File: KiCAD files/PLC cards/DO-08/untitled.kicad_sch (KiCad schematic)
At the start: 50 parts

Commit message: pcbs
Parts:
- gave numbers to parts that had none: 50

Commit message: pcbs
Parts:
- RN2, RN3: value 220 -> (none)
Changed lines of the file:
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@@
   (symbol (lib_id "Device:R_Network04") (at 200.66 24.638 0) (unit 1)
     (in_bom yes) (on_board yes) (fields_autoplaced)
-    (property "Reference" "RN3" (id 0) (at 205.232 23.6219 0)
+    (property "Reference" "RN3" (id 0) (at 205.74 23.6219 0)
       (effects (font (size 1.27 1.27)) (justify left))
     )
-    (property "Value" "220" (id 1) (at 205.232 26.1619 0)
+    (property "Value" "" (id 1) (at 205.74 26.1619 0)
       (effects (font (size 1.27 1.27)) (justify left))
     )
@@
   (symbol (lib_id "Device:R_Network04") (at 67.31 68.326 0) (unit 1)
     (in_bom yes) (on_board yes) (fields_autoplaced)
-    (property "Reference" "RN2" (id 0) (at 71.882 67.3099 0)
+    (property "Reference" "RN2" (id 0) (at 72.39 67.3099 0)
       (effects (font (size 1.27 1.27)) (justify left))
     )
-    (property "Value" "220" (id 1) (at 71.882 69.8499 0)
+    (property "Value" "" (id 1) (at 72.39 69.8499 0)
       (effects (font (size 1.27 1.27)) (justify left))
     )

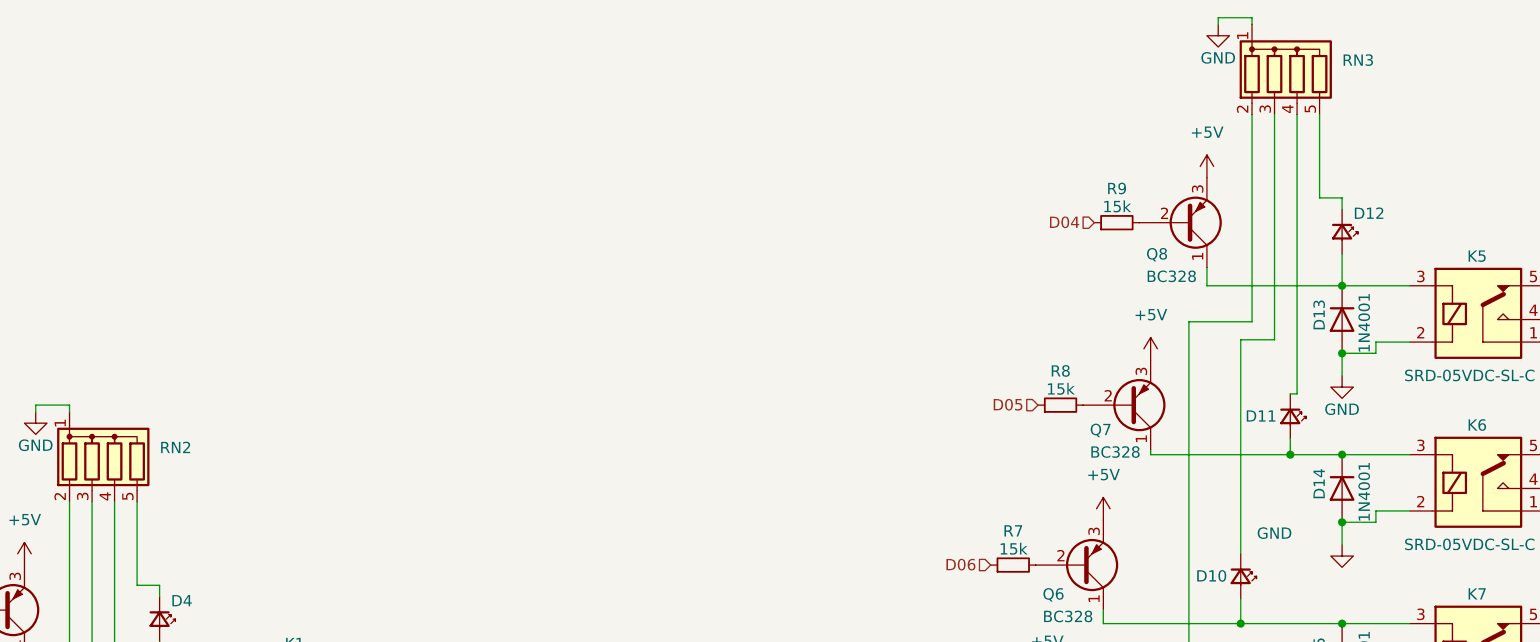
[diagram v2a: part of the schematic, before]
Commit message: DI & DO updates
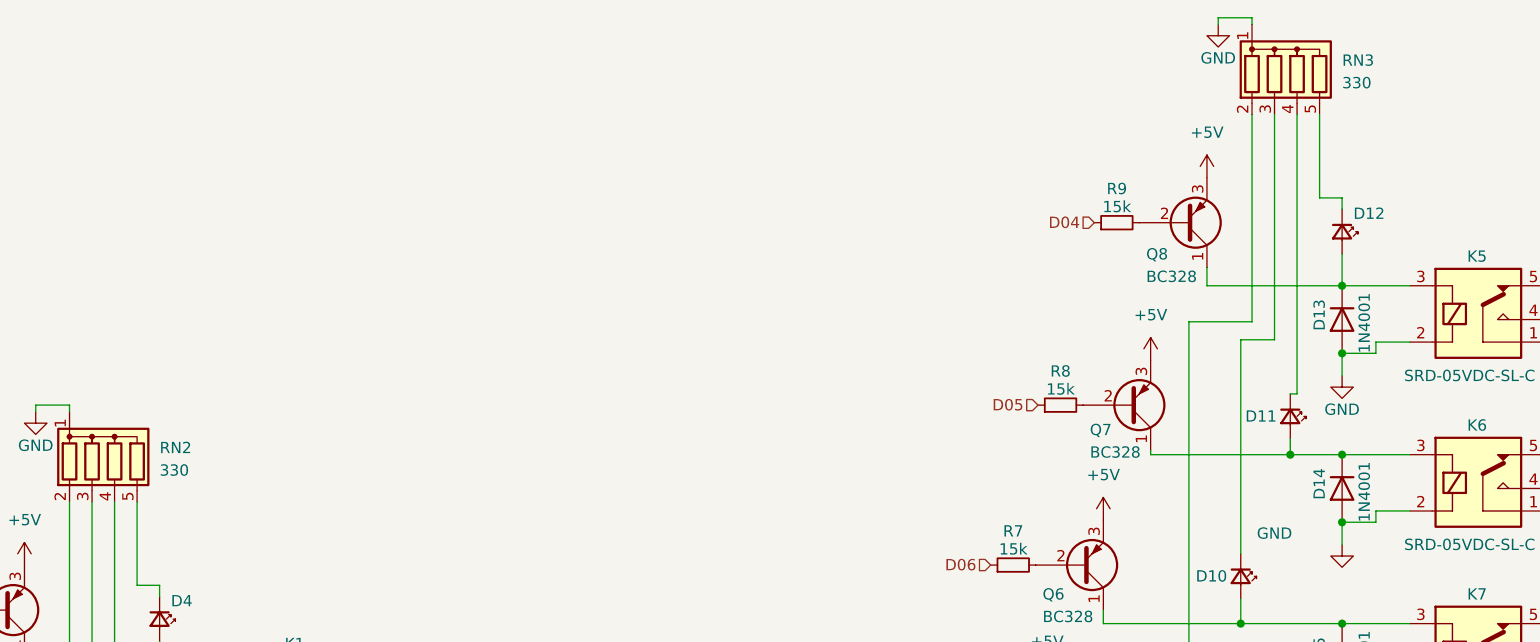
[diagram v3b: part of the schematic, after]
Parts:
- RN2, RN3: value (none) -> 330
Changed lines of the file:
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@@
       (effects (font (size 1.27 1.27)) (justify left))
     )
-    (property "Value" "" (id 1) (at 205.74 26.1619 0)
+    (property "Value" "330" (id 1) (at 205.74 26.1619 0)
       (effects (font (size 1.27 1.27)) (justify left))
     )
@@
       (effects (font (size 1.27 1.27)) (justify left))
     )
-    (property "Value" "" (id 1) (at 72.39 69.8499 0)
+    (property "Value" "330" (id 1) (at 72.39 69.8499 0)
       (effects (font (size 1.27 1.27)) (justify left))
     )
